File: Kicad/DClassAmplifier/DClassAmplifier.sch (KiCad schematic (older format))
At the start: 7 parts

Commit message: Finish off Main Part of Schematic
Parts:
- removed C?: 10uF, symbol Device:C_Small
- added C?: 10u 50V, Capacitor_SMD:C_1206_3216Metric_Pad1.33x1.80mm_HandSolder, symbol Device:C_Small
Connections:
- wire segments 20 -> 24
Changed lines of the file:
@@
 $Descr A4 11693 8268
 encoding utf-8
-Sheet 1 9
+Sheet 1 7
 Title ""
 Date ""
@@
 $EndDescr
 $Sheet
-S 7625 2800 875  300
+S 7700 3175 850  225
 U 60F78807
 F0 "OutputFilter" 50
 F1 "OutputFilter.sch" 50
-F2 "SIG_IN" I L 7625 2950 50
-F3 "SIG_OUT" O R 8500 2950 50
+F2 "SIG+" I L 7700 3250 50
+F3 "SIG-" I L 7700 3350 50
+F4 "SPEAKER+" O R 8550 3250 50
+F5 "SPEAKER-" O R 8550 3350 50
 $EndSheet
 $Comp
@@
 L Device:Speaker LS?
 U 1 1 60FD7EA0
-P 9550 3250
-F 0 "LS?" H 9720 3246 50  0000 L CNN
-F 1 "Speaker" H 9720 3155 50  0000 L CNN
-F 2 "" H 9550 3050 50  0001 C CNN
-F 3 "~" H 9540 3200 50  0001 C CNN
-	1    9550 3250
-	1    0    0    -1
-$EndComp
-$Sheet
-S 6000 1850 900  250
-U 60FDBAA4
-F0 "Feedback" 50
-F1 "Feedback.sch" 50
-$EndSheet
-$Sheet
-S 6000 2700 1000 550
-U 60FDBB90
-F0 "H-Bridge" 50
-F1 "H-Bridge.sch" 50
-F2 "PWM" I L 6000 2950 50
-F3 "V_OUT1" O R 7000 2950 50
-$EndSheet
+P 8850 3250
+F 0 "LS?" H 9020 3246 50  0000 L CNN
+F 1 "Speaker" H 9020 3155 50  0000 L CNN
+F 2 "" H 8850 3050 50  0001 C CNN
+F 3 "~" H 8840 3200 50  0001 C CNN
+	1    8850 3250
+	1    0    0    -1
+$EndComp
 $Comp
 L Mechanical:MountingHole H?
@@
 	1    0    0    -1
 $EndComp
-$Comp
-L Device:C_Small C?
-U 1 1 6101A94F
-P 8825 2025
-AR Path="/60FDBB90/6101A94F" Ref="C?"  Part="1"
-AR Path="/6101A94F" Ref="C?"  Part="1"
-F 0 "C?" H 8917 2071 50  0000 L CNN
-F 1 "10uF" H 8917 1980 50  0000 L CNN
-F 2 "" H 8825 2025 50  0001 C CNN
-F 3 "~" H 8825 2025 50  0001 C CNN
-	1    8825 2025
-	1    0    0    -1
-$EndComp
 Wire Wire Line
 	8825 2225 8825 2125
 Wire Wire Line
 	8825 1825 8825 1925
-Wire Wire Line
-	7000 2950 7625 2950
-$Sheet
-S 7625 3550 875  300
-U 610505A7
-F0 "sheet610505A2" 50
-F1 "OutputFilter.sch" 50
-F2 "SIG_IN" I L 7625 3700 50
-F3 "SIG_OUT" O R 8500 3700 50
-$EndSheet
-Wire Wire Line
-	7000 3700 7625 3700
-Wire Wire Line
-	8500 3700 8775 3700
-Wire Wire Line
-	8775 3350 9350 3350
-$Sheet
-S 6000 3450 1000 550
-U 6110CB49
-F0 "sheet6110CB45" 50
-F1 "H-Bridge.sch" 50
-F2 "PWM" I L 6000 3700 50
-F3 "V_OUT1" O R 7000 3700 50
-$EndSheet
-$Sheet
-S 4275 3150 1100 475
+$Sheet
+S 5400 3175 1150 225
 U 61113C55
 F0 "Comparator" 50
 F1 "Comparator.sch" 50
-F2 "PWM_OUT" O R 5375 3300 50
-F3 "INV_PWM_OUT" O R 5375 3450 50
-F4 "TRIANGLE_IN" I L 4275 3325 50
-F5 "SIG_IN" I L 4275 3450 50
-$EndSheet
-Wire Wire Line
-	5375 3450 5725 3450
-Wire Wire Line
-	5725 3450 5725 3700
-Wire Wire Line
-	5725 3700 6000 3700
-Wire Wire Line
-	6000 2950 5725 2950
-Wire Wire Line
-	5725 2950 5725 3300
-Wire Wire Line
-	5725 3300 5375 3300
-Wire Wire Line
-	9350 3250 8775 3250
-Wire Wire Line
-	8775 2950 8500 2950
-Wire Wire Line
-	8775 3250 8775 2950
-Wire Wire Line
-	8775 3350 8775 3700
-$Sheet
-S 2550 2800 1000 300
+F2 "PWM_OUT" O R 6550 3250 50
+F3 "INV_PWM_OUT" O R 6550 3350 50
+F4 "TRIANGLE_IN" I L 5400 3250 50
+F5 "SIG_IN" I L 5400 3350 50
+$EndSheet
+$Sheet
+S 3875 2950 1000 300
 U 6109BB03
 F0 "TriangleWave" 50
 F1 "TriangleWave.sch" 50
-F2 "TRIANGLE_OUT" O R 3550 2950 50
-$EndSheet
-$Sheet
-S 2550 3600 950  300
+F2 "TRIANGLE_OUT" O R 4875 3100 50
+F3 "VREF" I L 3875 3100 50
+$EndSheet
+Wire Wire Line
+	8550 3350 8650 3350
+Wire Wire Line
+	8550 3250 8650 3250
+$Sheet
+S 6675 3175 825  225
+U 60FDBB90
+F0 "H-Bridge" 50
+F1 "H-Bridge.sch" 50
+F2 "V_OUT+" O R 7500 3250 50
+F3 "PWM" I L 6675 3250 50
+F4 "INV_PWM" I L 6675 3350 50
+F5 "V_OUT-" O R 7500 3350 50
+$EndSheet
+Wire Wire Line
+	7500 3250 7700 3250
+Wire Wire Line
+	7700 3350 7500 3350
+Wire Wire Line
+	6550 3350 6675 3350
+Wire Wire Line
+	6550 3250 6675 3250
+Wire Wire Line
+	4875 3100 5150 3100
+Wire Wire Line
+	5150 3100 5150 3250
+Wire Wire Line
+	5150 3250 5400 3250
+Wire Wire Line
+	5400 3350 5150 3350
+Wire Wire Line
+	5150 3350 5150 3600
+Wire Wire Line
+	5150 3600 4825 3600
+Wire Wire Line
+	3800 3100 3875 3100
+$Sheet
+S 2325 3275 575  350
+U 611D4178
+F0 "Sheet611D4177" 50
+F1 "InputStage.sch" 50
+F2 "SIG_IN" I L 2325 3450 50
+F3 "SIG_OUT" O R 2900 3550 50
+F4 "VREF" O R 2900 3375 50
+$EndSheet
+$Sheet
+S 3875 3450 950  300
 U 610C616D
-F0 "SignalBias" 50
-F1 "SignalBias.sch" 50
-F2 "SIG_OUT" O R 3500 3750 50
-F3 "AUDIO_IN" I L 2550 3750 50
-$EndSheet
+F0 "LPF" 50
+F1 "LPF.sch" 50
+F2 "SIG_OUT" O R 4825 3600 50
+F3 "SIG_IN" I L 3875 3600 50
+$EndSheet
+Wire Wire Line
+	2900 3375 3800 3375
+Wire Wire Line
+	3800 3375 3800 3100
+Wire Wire Line
+	3700 3550 2900 3550
+Wire Wire Line
+	3875 3600 3700 3600
+Wire Wire Line
+	3700 3600 3700 3550
+$Comp
+L Device:C_Small C?
+U 1 1 61206AE9
+P 8825 2025
+AR Path="/60FDBB90/61206AE9" Ref="C?"  Part="1"
+AR Path="/610505AB/61206AE9" Ref="C?"  Part="1"
+AR Path="/6110CB49/61206AE9" Ref="C?"  Part="1"
+F 0 "C?" H 8917 2071 50  0000 L CNN
+F 1 "10u 50V" H 8917 1980 50  0000 L CNN
+F 2 "Capacitor_SMD:C_1206_3216Metric_Pad1.33x1.80mm_HandSolder" H 8825 2025 50  0001 C CNN
+F 3 "~" H 8825 2025 50  0001 C CNN
+F 4 "C2012X7R2A104K125AA" H 8825 2025 50  0001 C CNN "PN"
+F 5 "> 20nF" H 8825 2025 50  0001 C CNN "Notes"
+	1    8825 2025
+	-1   0    0    1
+$EndComp
 $EndSCHEMATC

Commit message: updates to schematic
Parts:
- gave numbers to parts that had none: 7
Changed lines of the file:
@@
 $EndSheet
 $Comp
-L power:GNDPWR #PWR?
+L power:GNDPWR #PWR0101
 U 1 1 60FD17D7
 P 1350 1050
-F 0 "#PWR?" H 1350 850 50  0001 C CNN
+F 0 "#PWR0101" H 1350 850 50  0001 C CNN
 F 1 "GNDPWR" H 1354 896 50  0000 C CNN
 F 2 "" H 1350 1000 50  0001 C CNN
@@
 $EndComp
 $Comp
-L power:GND #PWR?
+L power:GND #PWR0102
 U 1 1 60FD1A94
 P 1050 1050
-F 0 "#PWR?" H 1050 800 50  0001 C CNN
+F 0 "#PWR0102" H 1050 800 50  0001 C CNN
 F 1 "GND" H 1055 877 50  0000 C CNN
 F 2 "" H 1050 1050 50  0001 C CNN
@@
 $EndComp
 $Comp
-L Device:Net-Tie_2 NT?
+L Device:Net-Tie_2 NT1
 U 1 1 60FD21E0
 P 1200 950
-F 0 "NT?" H 1200 1131 50  0000 C CNN
+F 0 "NT1" H 1200 1131 50  0000 C CNN
 F 1 "Net-Tie_2" H 1200 1040 50  0000 C CNN
 F 2 "NetTie:NetTie-2_SMD_Pad2.0mm" H 1200 950 50  0001 C CNN
@@
 	1350 950  1350 1050
 $Comp
-L Device:Speaker LS?
+L Device:Speaker LS1
 U 1 1 60FD7EA0
 P 8850 3250
-F 0 "LS?" H 9020 3246 50  0000 L CNN
+F 0 "LS1" H 9020 3246 50  0000 L CNN
 F 1 "Speaker" H 9020 3155 50  0000 L CNN
 F 2 "" H 8850 3050 50  0001 C CNN
@@
 $EndComp
 $Comp
-L Mechanical:MountingHole H?
+L Mechanical:MountingHole H1
 U 1 1 60FDDA7B
 P 2100 900
-F 0 "H?" H 2200 991 50  0000 L CNN
+F 0 "H1" H 2200 991 50  0000 L CNN
 F 1 "MountingHole" H 2200 900 50  0000 L CNN
 F 2 "MountingHole:MountingHole_3.2mm_M3_ISO7380_Pad" H 2100 900 50  0001 C CNN
@@
 $EndComp
 $Comp
-L Mechanical:MountingHole H?
+L Mechanical:MountingHole H2
 U 1 1 60FDF5F8
 P 2100 1150
-F 0 "H?" H 2200 1241 50  0000 L CNN
+F 0 "H2" H 2200 1241 50  0000 L CNN
 F 1 "MountingHole" H 2200 1150 50  0000 L CNN
 F 2 "MountingHole:MountingHole_3.2mm_M3_ISO7380_Pad" H 2100 1150 50  0001 C CNN
@@
 $EndComp
 $Comp
-L Mechanical:MountingHole H?
+L Mechanical:MountingHole H3
 U 1 1 60FDFD61
 P 2800 900
-F 0 "H?" H 2900 991 50  0000 L CNN
+F 0 "H3" H 2900 991 50  0000 L CNN
 F 1 "MountingHole" H 2900 900 50  0000 L CNN
 F 2 "MountingHole:MountingHole_3.2mm_M3_ISO7380_Pad" H 2800 900 50  0001 C CNN
@@
 $EndComp
 $Comp
-L Mechanical:MountingHole H?
+L Mechanical:MountingHole H4
 U 1 1 60FDFFD3
 P 2800 1150
-F 0 "H?" H 2900 1241 50  0000 L CNN
+F 0 "H4" H 2900 1241 50  0000 L CNN
 F 1 "MountingHole" H 2900 1150 50  0000 L CNN
 F 2 "MountingHole:MountingHole_3.2mm_M3_ISO7380_Pad" H 2800 1150 50  0001 C CNN
@@
 M3 Mounting Holes
 $Comp
-L power:VDD #PWR?
+L power:VDD #PWR0103
 U 1 1 6101A943
 P 8825 1825
-F 0 "#PWR?" H 8825 1675 50  0001 C CNN
+F 0 "#PWR0103" H 8825 1675 50  0001 C CNN
 F 1 "VDD" H 8840 1998 50  0000 C CNN
 F 2 "" H 8825 1825 50  0001 C CNN
@@
 $EndComp
 $Comp
-L power:GNDPWR #PWR?
+L power:GNDPWR #PWR0104
 U 1 1 6101A949
 P 8825 2225
-F 0 "#PWR?" H 8825 2025 50  0001 C CNN
+F 0 "#PWR0104" H 8825 2025 50  0001 C CNN
 F 1 "GNDPWR" H 8829 2071 50  0000 C CNN
 F 2 "" H 8825 2175 50  0001 C CNN
@@
 AR Path="/610505AB/61206AE9" Ref="C?"  Part="1"
 AR Path="/6110CB49/61206AE9" Ref="C?"  Part="1"
-F 0 "C?" H 8917 2071 50  0000 L CNN
+AR Path="/61206AE9" Ref="C2"  Part="1"
+F 0 "C2" H 8917 2071 50  0000 L CNN
 F 1 "10u 50V" H 8917 1980 50  0000 L CNN
 F 2 "Capacitor_SMD:C_1206_3216Metric_Pad1.33x1.80mm_HandSolder" H 8825 2025 50  0001 C CNN

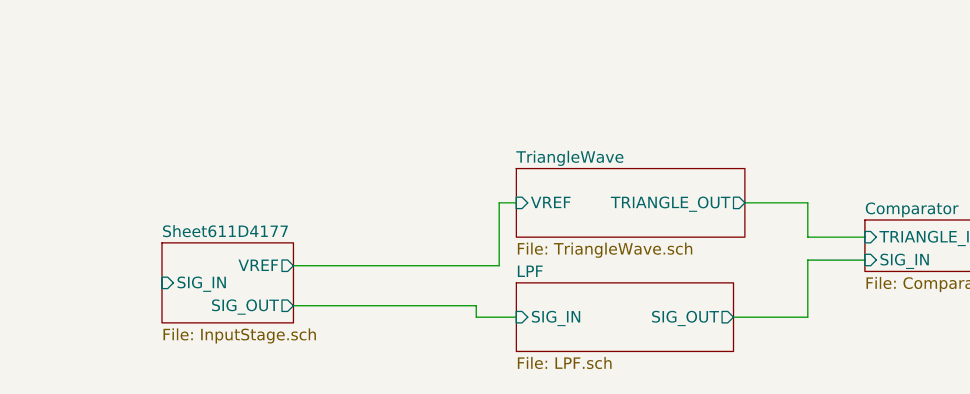
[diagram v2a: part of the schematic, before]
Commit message: Update Opamp for Input Filter
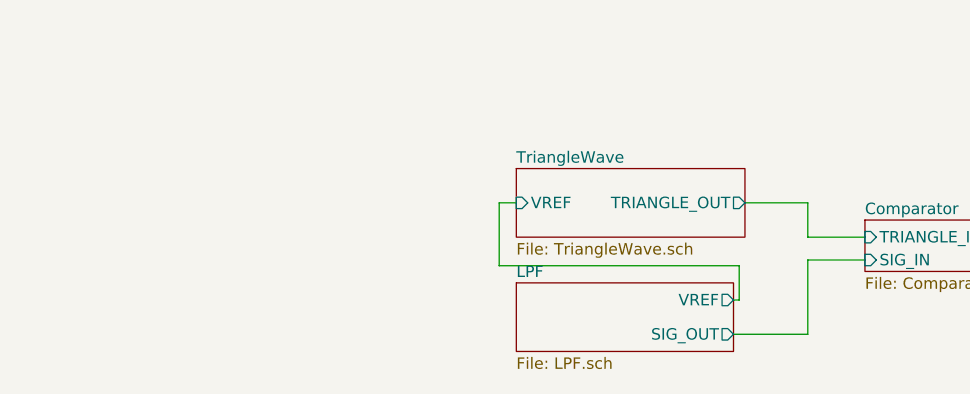
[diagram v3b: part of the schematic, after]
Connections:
- wire segments 24 -> 23
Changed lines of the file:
@@
 $Descr A4 11693 8268
 encoding utf-8
-Sheet 1 7
+Sheet 1 6
 Title ""
 Date ""
@@
 	5400 3350 5150 3350
 Wire Wire Line
-	5150 3350 5150 3600
-Wire Wire Line
-	5150 3600 4825 3600
-Wire Wire Line
 	3800 3100 3875 3100
-$Sheet
-S 2325 3275 575  350
-U 611D4178
-F0 "Sheet611D4177" 50
-F1 "InputStage.sch" 50
-F2 "SIG_IN" I L 2325 3450 50
-F3 "SIG_OUT" O R 2900 3550 50
-F4 "VREF" O R 2900 3375 50
-$EndSheet
 $Sheet
 S 3875 3450 950  300
@@
 F0 "LPF" 50
 F1 "LPF.sch" 50
-F2 "SIG_OUT" O R 4825 3600 50
-F3 "SIG_IN" I L 3875 3600 50
-$EndSheet
-Wire Wire Line
-	2900 3375 3800 3375
+F2 "SIG_OUT" O R 4825 3675 50
+F3 "VREF" O R 4825 3525 50
+$EndSheet
 Wire Wire Line
 	3800 3375 3800 3100
-Wire Wire Line
-	3700 3550 2900 3550
-Wire Wire Line
-	3875 3600 3700 3600
-Wire Wire Line
-	3700 3600 3700 3550
 $Comp
 L Device:C_Small C?
@@
 	-1   0    0    1
 $EndComp
+Wire Wire Line
+	5150 3350 5150 3675
+Wire Wire Line
+	4825 3675 5150 3675
+Wire Wire Line
+	4825 3525 4850 3525
+Wire Wire Line
+	4850 3525 4850 3375
+Wire Wire Line
+	4850 3375 3800 3375
 $EndSCHEMATC

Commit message: Added footprints to schematic
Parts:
- removed LS1: Speaker, symbol Device:Speaker
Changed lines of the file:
@@
 	1350 950  1350 1050
-$Comp
-L Device:Speaker LS1
-U 1 1 60FD7EA0
-P 8850 3250
-F 0 "LS1" H 9020 3246 50  0000 L CNN
-F 1 "Speaker" H 9020 3155 50  0000 L CNN
-F 2 "" H 8850 3050 50  0001 C CNN
-F 3 "~" H 8840 3200 50  0001 C CNN
-	1    8850 3250
-	1    0    0    -1
-$EndComp
 $Comp
 L Mechanical:MountingHole H1

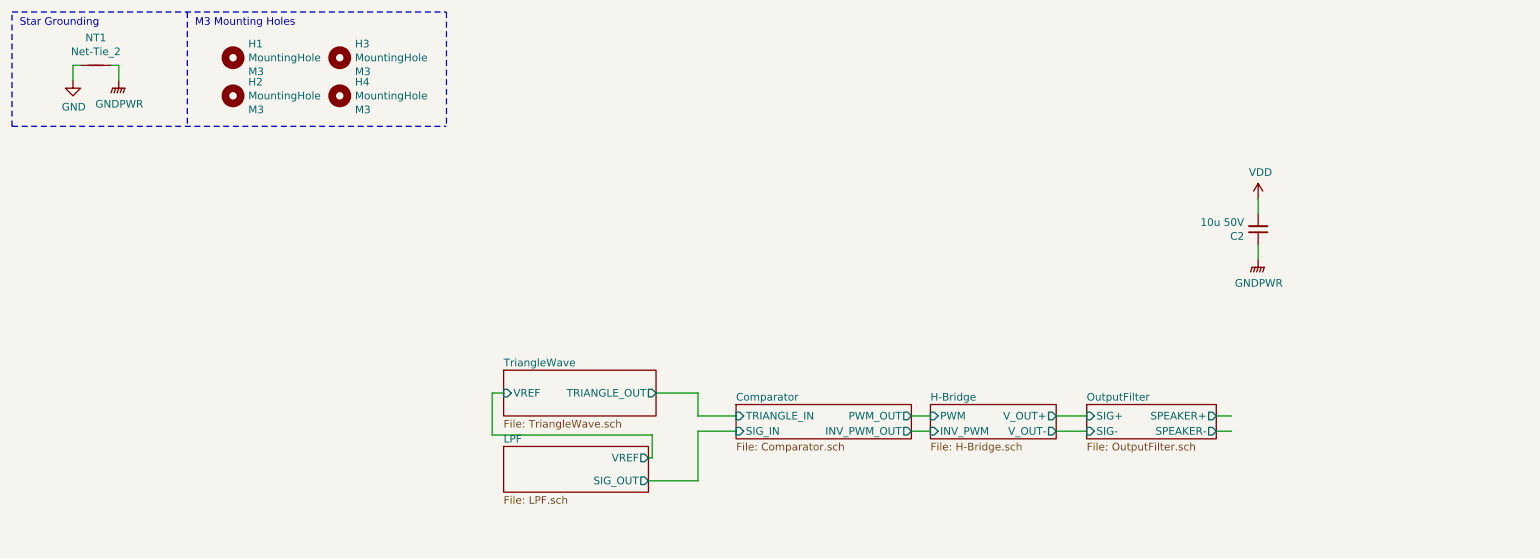
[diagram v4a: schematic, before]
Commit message: Add Test Points
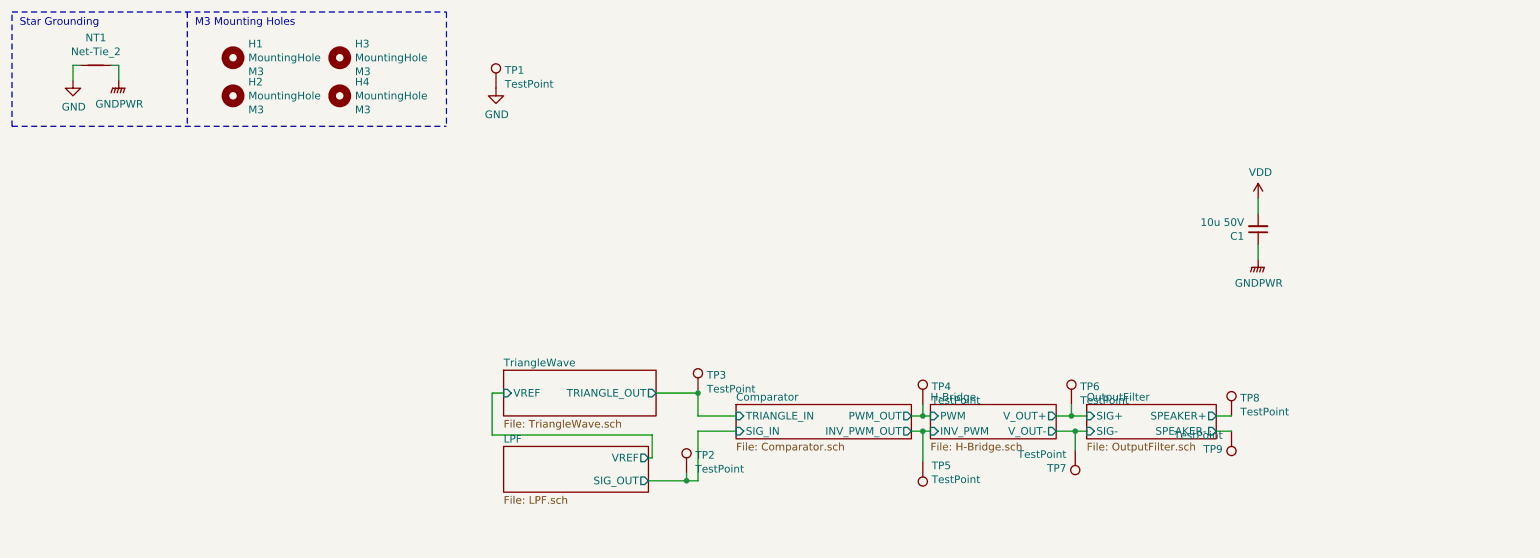
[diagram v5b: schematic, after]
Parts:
- added TP1, TP2, TP3, TP4, TP5, TP6, TP7, TP8, TP9: TestPoint, TestPoint:TestPoint_Pad_D2.0mm, symbol Connector:TestPoint
- renumbered C2 to C1
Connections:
- wire segments 23 -> 33
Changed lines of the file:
@@
 $EndSheet
 $Comp
-L power:GNDPWR #PWR0101
+L power:GNDPWR #PWR02
 U 1 1 60FD17D7
 P 1350 1050
-F 0 "#PWR0101" H 1350 850 50  0001 C CNN
+F 0 "#PWR02" H 1350 850 50  0001 C CNN
 F 1 "GNDPWR" H 1354 896 50  0000 C CNN
 F 2 "" H 1350 1000 50  0001 C CNN
@@
 $EndComp
 $Comp
-L power:GND #PWR0102
+L power:GND #PWR01
 U 1 1 60FD1A94
 P 1050 1050
-F 0 "#PWR0102" H 1050 800 50  0001 C CNN
+F 0 "#PWR01" H 1050 800 50  0001 C CNN
 F 1 "GND" H 1055 877 50  0000 C CNN
 F 2 "" H 1050 1050 50  0001 C CNN
@@
 M3 Mounting Holes
 $Comp
-L power:VDD #PWR0103
+L power:VDD #PWR04
 U 1 1 6101A943
 P 8825 1825
-F 0 "#PWR0103" H 8825 1675 50  0001 C CNN
+F 0 "#PWR04" H 8825 1675 50  0001 C CNN
 F 1 "VDD" H 8840 1998 50  0000 C CNN
 F 2 "" H 8825 1825 50  0001 C CNN
@@
 $EndComp
 $Comp
-L power:GNDPWR #PWR0104
+L power:GNDPWR #PWR05
 U 1 1 6101A949
 P 8825 2225
-F 0 "#PWR0104" H 8825 2025 50  0001 C CNN
+F 0 "#PWR05" H 8825 2025 50  0001 C CNN
 F 1 "GNDPWR" H 8829 2071 50  0000 C CNN
 F 2 "" H 8825 2175 50  0001 C CNN
@@
 $EndSheet
 Wire Wire Line
-	7500 3250 7700 3250
-Wire Wire Line
-	7700 3350 7500 3350
-Wire Wire Line
-	6550 3350 6675 3350
-Wire Wire Line
-	6550 3250 6675 3250
+	7500 3250 7600 3250
+Wire Wire Line
+	7700 3350 7625 3350
+Wire Wire Line
+	6550 3350 6625 3350
+Wire Wire Line
+	6550 3250 6625 3250
 Wire Wire Line
 	4875 3100 5150 3100
@@
 AR Path="/610505AB/61206AE9" Ref="C?"  Part="1"
 AR Path="/6110CB49/61206AE9" Ref="C?"  Part="1"
-AR Path="/61206AE9" Ref="C2"  Part="1"
-F 0 "C2" H 8917 2071 50  0000 L CNN
+AR Path="/61206AE9" Ref="C1"  Part="1"
+F 0 "C1" H 8917 2071 50  0000 L CNN
 F 1 "10u 50V" H 8917 1980 50  0000 L CNN
 F 2 "Capacitor_SMD:C_1206_3216Metric_Pad1.33x1.80mm_HandSolder" H 8825 2025 50  0001 C CNN
@@
 	5150 3350 5150 3675
 Wire Wire Line
-	4825 3675 5150 3675
+	4825 3675 5075 3675
 Wire Wire Line
 	4825 3525 4850 3525
@@
 Wire Wire Line
 	4850 3375 3800 3375
+$Comp
+L Connector:TestPoint TP3
+U 1 1 610FFA0B
+P 5150 3100
+F 0 "TP3" H 5208 3218 50  0000 L CNN
+F 1 "TestPoint" H 5208 3127 50  0000 L CNN
+F 2 "TestPoint:TestPoint_Pad_D2.0mm" H 5350 3100 50  0001 C CNN
+F 3 "~" H 5350 3100 50  0001 C CNN
+	1    5150 3100
+	1    0    0    -1
+$EndComp
+Connection ~ 5150 3100
+$Comp
+L Connector:TestPoint TP2
+U 1 1 611007B2
+P 5075 3625
+F 0 "TP2" H 5133 3743 50  0000 L CNN
+F 1 "TestPoint" H 5133 3652 50  0000 L CNN
+F 2 "TestPoint:TestPoint_Pad_D2.0mm" H 5275 3625 50  0001 C CNN
+F 3 "~" H 5275 3625 50  0001 C CNN
+	1    5075 3625
+	1    0    0    -1
+$EndComp
+$Comp
+L Connector:TestPoint TP4
+U 1 1 61100CCA
+P 6625 3175
+F 0 "TP4" H 6683 3293 50  0000 L CNN
+F 1 "TestPoint" H 6683 3202 50  0000 L CNN
+F 2 "TestPoint:TestPoint_Pad_D2.0mm" H 6825 3175 50  0001 C CNN
+F 3 "~" H 6825 3175 50  0001 C CNN
+	1    6625 3175
+	1    0    0    -1
+$EndComp
+$Comp
+L Connector:TestPoint TP5
+U 1 1 611012C1
+P 6625 3550
+F 0 "TP5" H 6567 3576 50  0000 R CNN
+F 1 "TestPoint" H 6567 3667 50  0000 R CNN
+F 2 "TestPoint:TestPoint_Pad_D2.0mm" H 6825 3550 50  0001 C CNN
+F 3 "~" H 6825 3550 50  0001 C CNN
+	1    6625 3550
+	-1   0    0    1
+$EndComp
+Wire Wire Line
+	5075 3625 5075 3675
+Connection ~ 5075 3675
+Wire Wire Line
+	5075 3675 5150 3675
+Wire Wire Line
+	6625 3550 6625 3350
+Connection ~ 6625 3350
+Wire Wire Line
+	6625 3350 6675 3350
+Connection ~ 6625 3250
+Wire Wire Line
+	6625 3250 6675 3250
+Wire Wire Line
+	6625 3175 6625 3250
+$Comp
+L Connector:TestPoint TP8
+U 1 1 61104270
+P 8650 3250
+F 0 "TP8" H 8708 3368 50  0000 L CNN
+F 1 "TestPoint" H 8708 3277 50  0000 L CNN
+F 2 "TestPoint:TestPoint_Pad_D2.0mm" H 8850 3250 50  0001 C CNN
+F 3 "~" H 8850 3250 50  0001 C CNN
+	1    8650 3250
+	1    0    0    -1
+$EndComp
+$Comp
+L Connector:TestPoint TP9
+U 1 1 61104B4E
+P 8650 3350
+F 0 "TP9" H 8708 3468 50  0000 L CNN
+F 1 "TestPoint" H 8708 3377 50  0000 L CNN
+F 2 "TestPoint:TestPoint_Pad_D2.0mm" H 8850 3350 50  0001 C CNN
+F 3 "~" H 8850 3350 50  0001 C CNN
+	1    8650 3350
+	-1   0    0    1
+$EndComp
+$Comp
+L Connector:TestPoint TP7
+U 1 1 61105E39
+P 7625 3475
+F 0 "TP7" H 7683 3593 50  0000 L CNN
+F 1 "TestPoint" H 7683 3502 50  0000 L CNN
+F 2 "TestPoint:TestPoint_Pad_D2.0mm" H 7825 3475 50  0001 C CNN
+F 3 "~" H 7825 3475 50  0001 C CNN
+	1    7625 3475
+	-1   0    0    1
+$EndComp
+Wire Wire Line
+	7625 3475 7625 3350
+Connection ~ 7625 3350
+Wire Wire Line
+	7625 3350 7500 3350
+$Comp
+L Connector:TestPoint TP6
+U 1 1 61106CFC
+P 7600 3175
+F 0 "TP6" H 7658 3293 50  0000 L CNN
+F 1 "TestPoint" H 7658 3202 50  0000 L CNN
+F 2 "TestPoint:TestPoint_Pad_D2.0mm" H 7800 3175 50  0001 C CNN
+F 3 "~" H 7800 3175 50  0001 C CNN
+	1    7600 3175
+	1    0    0    -1
+$EndComp
+Wire Wire Line
+	7600 3175 7600 3250
+Connection ~ 7600 3250
+Wire Wire Line
+	7600 3250 7700 3250
+$Comp
+L Connector:TestPoint TP1
+U 1 1 611138A1
+P 3825 1100
+F 0 "TP1" H 3883 1218 50  0000 L CNN
+F 1 "TestPoint" H 3883 1127 50  0000 L CNN
+F 2 "TestPoint:TestPoint_Pad_D2.0mm" H 4025 1100 50  0001 C CNN
+F 3 "~" H 4025 1100 50  0001 C CNN
+	1    3825 1100
+	1    0    0    -1
+$EndComp
+$Comp
+L power:GND #PWR03
+U 1 1 61114095
+P 3825 1100
+F 0 "#PWR03" H 3825 850 50  0001 C CNN
+F 1 "GND" H 3830 927 50  0000 C CNN
+F 2 "" H 3825 1100 50  0001 C CNN
+F 3 "" H 3825 1100 50  0001 C CNN
+	1    3825 1100
+	1    0    0    -1
+$EndComp
 $EndSCHEMATC

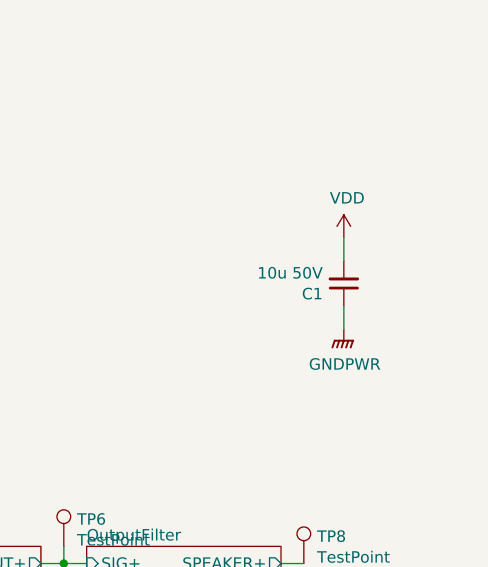
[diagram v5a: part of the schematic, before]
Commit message: Add 10m Resevoir Cap
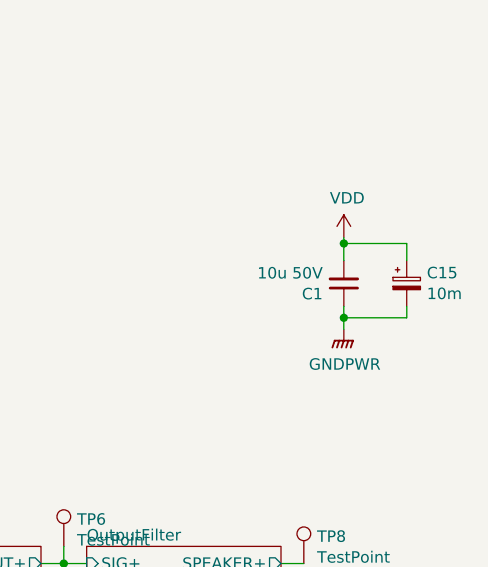
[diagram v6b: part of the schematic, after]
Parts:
- added C15: 10m, Capacitor_THT:CP_Radial_D18.0mm_P7.50mm, symbol Device:CP_Small
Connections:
- net GNDPWR: now also C15.2
- net VDD: now also C15.1
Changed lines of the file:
@@
 $EndComp
 Wire Wire Line
-	8825 2225 8825 2125
-Wire Wire Line
-	8825 1825 8825 1925
+	8825 2225 8825 2175
+Wire Wire Line
+	8825 1825 8825 1850
 $Sheet
 S 5400 3175 1150 225
@@
 	1    0    0    -1
 $EndComp
+$Comp
+L Device:CP_Small C15
+U 1 1 61112A42
+P 9100 2025
+F 0 "C15" H 9188 2071 50  0000 L CNN
+F 1 "10m" H 9188 1980 50  0000 L CNN
+F 2 "Capacitor_THT:CP_Radial_D18.0mm_P7.50mm" H 9100 2025 50  0001 C CNN
+F 3 "~" H 9100 2025 50  0001 C CNN
+	1    9100 2025
+	1    0    0    -1
+$EndComp
+Wire Wire Line
+	9100 2125 9100 2175
+Wire Wire Line
+	9100 2175 8825 2175
+Connection ~ 8825 2175
+Wire Wire Line
+	8825 2175 8825 2125
+Wire Wire Line
+	9100 1925 9100 1850
+Wire Wire Line
+	9100 1850 8825 1850
+Connection ~ 8825 1850
+Wire Wire Line
+	8825 1850 8825 1925
 $EndSCHEMATC
